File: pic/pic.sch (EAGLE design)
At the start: 33 parts, among them IC1 PIC16F877P, IC2 7805T, IC3 MAX233, Q1 16MHz, Q2 200MHz

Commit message: Schematic format update
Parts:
- added C7: 47μF, rcl:CPOL-EUE2.5-5
- added C8, C9: 15pF, rcl:CPOL-EUE2.5-5
- added F2: (no value), fuse:F457
- added IC4: 7805T, adafruit:7805T
- added IC5: MAX233, maxim:MAX233
- added J1: (no value), con-jack:JACK-PLUG1
- added J4: (no value), con-amp:520243-3
- added JP2: (no value), jumper:JP4Q
- added LED10: GREEN, adafruit:LED5MM
- added LED11: YELLOW, adafruit:LED5MM
- added LED12: RED, adafruit:LED5MM
- added LED7, LED8, LED9: (no value), adafruit:LED5MM
- added Q3: 16MHz, adafruit:CRYSTALHC49U-H
- added R11: 470, rcl:R-EU_0207/10
- added R12, R13: (no value), eagle-ltspice:R0207/10
- added R14: (no value), rcl:R-TRIMM3296X
- added R15, R16, R17, R18, R19: 470, eagle-ltspice:R0207/10
- added SW3, SW4: (no value), adafruit:SWITCH_PUSHBUTTONEVQ-PE
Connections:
- new net N$10: C7.+, IC4.VI, J1.3
- new net N$19: IC4.GND, J1.2
- new net N$20: F2.1, IC4.VO
- new net N$21: LED7.C, R11.2
- new net N$22: IC5G$1.R1IN, JP2.1, JP2.7
- new net N$23: IC5G$1.T1OUT, JP2.3, JP2.5
- new net N$24: J4.2, JP2.2, JP2.4
- new net N$25: J4.3, JP2.6, JP2.8
- new net N$26: IC5G$1.V-@1, IC5G$1.V-@2
- new net N$27: IC5G$1.C2-@1, IC5G$1.C2-@2
- new net N$28: IC5G$1.C2+@1, IC5G$1.C2+@2
- new net N$29: LED8.C, R15.1
- new net N$30: LED9.C, R16.1
- new net N$31: LED10.C, R17.1
- new net N$32: LED11.C, R18.1
- new net N$33: LED12.C, R19.1
- new net OSC3: C9.+, Q3.2
- new net OSC4: C8.+, Q3.1
- net A0: now also R14.S
- net A4: now also R13.1, SW4.P$2
- net A5: now also R17.2
- net B4: now also R18.2
- net B5: now also R19.2
- net C6: now also IC5G$1.T1IN
- net C7: now also IC5G$1.R1OUT
- net GND: now also C7.-, C8.-, C9.-, J4.5, R11.1, R14.E, SW3.P$1, SW4.P$1
- net LRX0: now also R16.2
- net LTX0: now also R15.2
- net RESET: now also R12.1, SW3.P$2
- net VCC: now also F2.2, LED10.A, LED11.A, LED12.A, LED7.A, LED8.A, LED9.A, R12.2, R13.2, R14.A

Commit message: 26/9/17 - LCD + PIC HEADER - EDITS TO RS232
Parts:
- removed J4: (no value), con-amp:520243-3
- removed SW3, SW4: (no value), adafruit:SWITCH_PUSHBUTTONEVQ-PE
- added C10: (no value), capacitor-wima:C5/5.5
- added C11, C12: 15pF, capacitor-wima:C5/5.5
- added C13: 1μF, rcl:CPOL-EUE2.5-5
- added IC6: PIC16F877P, microchip:PIC16F877P
- added J5: (no value), con-amp:520243-3
- added JP3: (no value), pinhead:PINHD-1X16
- added JP4: (no value), adafruit:PINHD-2X20
- added LED13: GREEN, adafruit:LED5MM
- added LED14: RED, adafruit:LED5MM
- added Q4: 200MHz, adafruit:CRYSTALHC49U-H
- added R20: 330, resistor:R-EU_0207/10
- added R21, R22: 470, resistor:R-EU_0207/10
- added R23: 10K, rcl:R-TRIMM3296X
- added R24: 100, eagle-ltspice:R0207/10
- added S1, S2: (no value), switch-omron:10-XX
- added X1: (no value), con-subd:F09HP
- R12, R13: value (none) -> 47K
- R14: value (none) -> 10K
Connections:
- removed net OSC3: C9.+, Q3.2
- removed net OSC4: C8.+, Q3.1
- new net 0SC1: JP4.14
- new net N$34: C12.2, Q4.1, R20.1
- new net N$35: LED13.A, R21.1
- new net N$36: LED14.A, R22.1
- new net N$38: JP3.3, R23.S
- new net N$45: JP3.15, R24.2
- new net N$46: C13.+, IC5P.VCC
- net A0: now also IC6.RA0/AN0, JP4.2
- net A1: now also IC6.RA1/AN1, JP4.3
- net A2: now also IC6.RA2/AN2, JP4.4
- net A3: now also IC6.RA3/AN3, JP4.5
- net A4: now also IC6.RA4/T0CKI, JP4.6, S2.S1; no longer SW4.P$2
- net A5: now also IC6.RA5/AN4, JP4.7
- net B0: now also IC6.INT/RB0, JP4.33
- net B1: now also IC6.RB1, JP4.34
- net B2: now also IC6.RB2, JP4.35
- net B3: now also IC6.PGM/RB3, JP4.36
- net B4: now also IC6.RB4, J5.4, JP4.37
- net B5: now also IC6.RB5, JP4.38
- net B6: now also IC6.PGC/RB6, J5.5, JP4.39
- net B7: now also IC6.PGD/RB7, J5.6, JP4.40
- net C0: now also IC6.RC0/T1OSO, JP4.15
- net C1: now also IC6.RC1/T1OSI, JP4.16
- net C2: now also IC6.RC2/CCP1, JP4.17
- net C3: now also IC6.RC3/SCK, JP4.18
- net C4: now also IC6.SDI/RC4, JP4.23
- net C5: now also IC6.SDO/RC5, JP4.24
- net C6: now also IC6.TX/RC6, JP4.25, LED13.C
- net C7: now also IC6.RX/RC7, JP4.26, LED14.C
- net D0: now also IC6.RD0/PSP0, JP3.6, JP4.19
- net D1: now also IC6.RD1/PSP1, JP3.4, JP4.20
- net D2: now also IC6.RD2/PSP2, JP3.5, JP4.21
- net D3: now also IC6.RD3/PSP3, JP4.22
- net D4: now also IC6.PSP4/RD4, JP3.11, JP4.27
- net D5: now also IC6.PSP5/RD5, JP3.12, JP4.28
- net D6: now also IC6.PSP6/RD6, JP3.13, JP4.29
- net D7: now also IC6.PSP7/RD7, JP3.14, JP4.30
- net E0: now also IC6.RE0/!RD/AN5, JP4.8
- net E1: now also IC6.RE1/!WR/AN6, JP4.9
- net E2: now also IC6.RE2/!CS/AN7, JP4.10
- net GND: now also C10.2, C11.1, C12.1, IC4.GND, IC6.VSS, IC6.VSS@1, J1.1, J1.2, J5.3, JP3.1, JP3.10, JP3.16, JP3.7, JP3.8, JP3.9, JP4.12, JP4.31, R21.2, R22.2, R23.A, S1.P1, S2.P1, X1.5; no longer J4.5, SW3.P$1, SW4.P$1
- net N$19: now also IC5P.GND@1, IC5P.GND@2; no longer IC4.GND, J1.2
- net N$24: now also X1.2; no longer J4.2
- net N$25: now also X1.3; no longer J4.3
- net OSC1: now also C11.2, C9.+, IC6.OSC1/CLKIN, Q3.2, Q4.2
- net OSC2: now also C8.+, IC6.OSC2/CLKOUT, JP4.13, Q3.1, R20.2
- net RESET: now also IC6.!MCLR/THV, J5.1, JP4.1, S1.S1; no longer SW3.P$2
- net VCC: now also C10.1, C13.-, IC6.VDD, IC6.VDD@1, J5.2, JP3.2, JP4.11, JP4.32, R23.E, R24.1

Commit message: Finished Schematic
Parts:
- removed C10: (no value), capacitor-wima:C5/5.5
- removed C11, C12: 15pF, capacitor-wima:C5/5.5
- removed C6: 15pF, rcl:CPOL-EUE2.5-5
- removed F1: (no value), fuse:F457
- removed IC2: 7805T, adafruit:7805T
- removed IC3: MAX233, maxim:MAX233
- removed IC6: PIC16F877P, microchip:PIC16F877P
- removed J2: (no value), con-amp:520243-3
- removed J3: (no value), con-jack:JACK-PLUG1
- removed LED1, LED2, LED3: (no value), adafruit:LED5MM
- removed LED4: GREEN, adafruit:LED5MM
- removed LED5: YELLOW, adafruit:LED5MM
- removed LED6: RED, adafruit:LED5MM
- removed Q1: 16MHz, adafruit:CRYSTALHC49U-H
- removed Q4: 200MHz, adafruit:CRYSTALHC49U-H
- removed R10, R6, R7, R8, R9: 470, eagle-ltspice:R0207/10
- removed R20: 330, resistor:R-EU_0207/10
- removed R3, R4: (no value), eagle-ltspice:R0207/10
- removed R5: (no value), rcl:R-TRIMM3296X
- removed SW1, SW2: (no value), adafruit:SWITCH_PUSHBUTTONEVQ-PE
- added IC7: PCA82C250, micro-philips:PCA82C250
- added U1: MCP2510P, microchip_can:MCP2510P
- added X2, X3: (no value), con-subd:F09HP
- C4: value 47μF -> 15μF
- C5: value 15pF -> 15μF
- JP1: device jumper:JP4Q -> jumper:JP1Q
- R2: device rcl:R-EU_0207/10 -> eagle-ltspice:R0207/10
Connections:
- removed net N$11: LED2.C, R6.1
- removed net N$12: IC3G$1.V-@1, IC3G$1.V-@2
- removed net N$13: IC3G$1.C2-@1, IC3G$1.C2-@2
- removed net N$14: IC3G$1.C2+@1, IC3G$1.C2+@2
- removed net N$15: LED3.C, R7.1
- removed net N$16: LED4.C, R8.1
- removed net N$17: LED5.C, R9.1
- removed net N$18: LED6.C, R10.1
- removed net N$34: C12.2, Q4.1, R20.1
- removed net N$5: IC3G$1.R1IN, JP1.1, JP1.7
- removed net N$6: LED1.C, R2.2
- removed net N$7: IC3G$1.T1OUT, JP1.3, JP1.5
- removed net N$8: J2.2, JP1.2, JP1.4
- removed net N$9: J2.3, JP1.6, JP1.8
- new net 0SC2: U1>NAME.OSC2
- net A0: no longer IC6.RA0/AN0, R5.S
- net A1: no longer IC6.RA1/AN1
- net A2: no longer IC6.RA2/AN2
- net A3: no longer IC6.RA3/AN3
- net A4: no longer IC6.RA4/T0CKI, R4.1, SW2.P$2
- net A5: no longer IC6.RA5/AN4, R8.2
- net B0: now also U1>NAME.INT; no longer IC6.INT/RB0
- net B1: no longer IC6.RB1
- net B2: no longer IC6.RB2
- net B3: no longer IC6.PGM/RB3
- net B4: no longer IC6.RB4, R9.2
- net B5: no longer IC6.RB5, R10.2
- net B6: no longer IC6.PGC/RB6
- net B7: no longer IC6.PGD/RB7
- net C0: no longer IC6.RC0/T1OSO
- net C1: no longer IC6.RC1/T1OSI
- net C2: now also U1>NAME.CS; no longer IC6.RC2/CCP1
- net C3: now also U1>NAME.SCK; no longer IC6.RC3/SCK
- net C4: now also U1>NAME.SO; no longer IC6.SDI/RC4
- net C5: now also U1>NAME.SI; no longer IC6.SDO/RC5
- net C6: no longer IC3G$1.T1IN, IC6.TX/RC6
- net C7: no longer IC3G$1.R1OUT, IC6.RX/RC7
- net D0: no longer IC6.RD0/PSP0
- net D1: no longer IC6.RD1/PSP1
- net D2: no longer IC6.RD2/PSP2
- net D3: no longer IC6.RD3/PSP3
- net D4: no longer IC6.PSP4/RD4
- net D5: no longer IC6.PSP5/RD5
- net D6: no longer IC6.PSP6/RD6
- net D7: no longer IC6.PSP7/RD7
- net E0: no longer IC6.RE0/!RD/AN5
- net E1: no longer IC6.RE1/!WR/AN6
- net E2: no longer IC6.RE2/!CS/AN7
- net GND: now also IC7.GND, IC7.RS, S1.P, S2.P, U1P.VSS, X2.6, X3.6; no longer C10.2, C11.1, C12.1, C6.-, IC6.VSS, IC6.VSS@1, J2.5, R2.1, R5.E, SW1.P$1, SW2.P$1
- net LRX0: now also IC7.TXD, U1>NAME.TXCAN; no longer R7.2
- net LTX0: now also IC7.RXD, U1>NAME.RXCAN; no longer R6.2
- net N$1: now also JP1.2, R2.2; no longer C4.+, IC2.VI, J3.3
- net N$3: now also IC7.CANL, R2.1, X2.2, X3.2; no longer IC2.GND, J3.2
- net N$4: now also IC7.CANH, JP1.1, X2.7, X3.7; no longer F1.1, IC2.VO
- net OSC1: now also U1>NAME.OSC1; no longer C11.2, C6.+, IC6.OSC1/CLKIN, Q1.2, Q4.2
- net OSC2: no longer C5.+, IC6.OSC2/CLKOUT, Q1.1, R20.2
- net RESET: now also S1.S, U1>NAME.RESET; no longer IC6.!MCLR/THV, R3.1, SW1.P$2
- net VCC: now also C4.+, C5.+, IC7.VCC, U1P.VDD, X2.9, X3.9; no longer C10.1, F1.2, IC6.VDD, IC6.VDD@1, LED1.A, LED2.A, LED3.A, LED4.A, LED5.A, LED6.A, R3.2, R4.2, R5.A

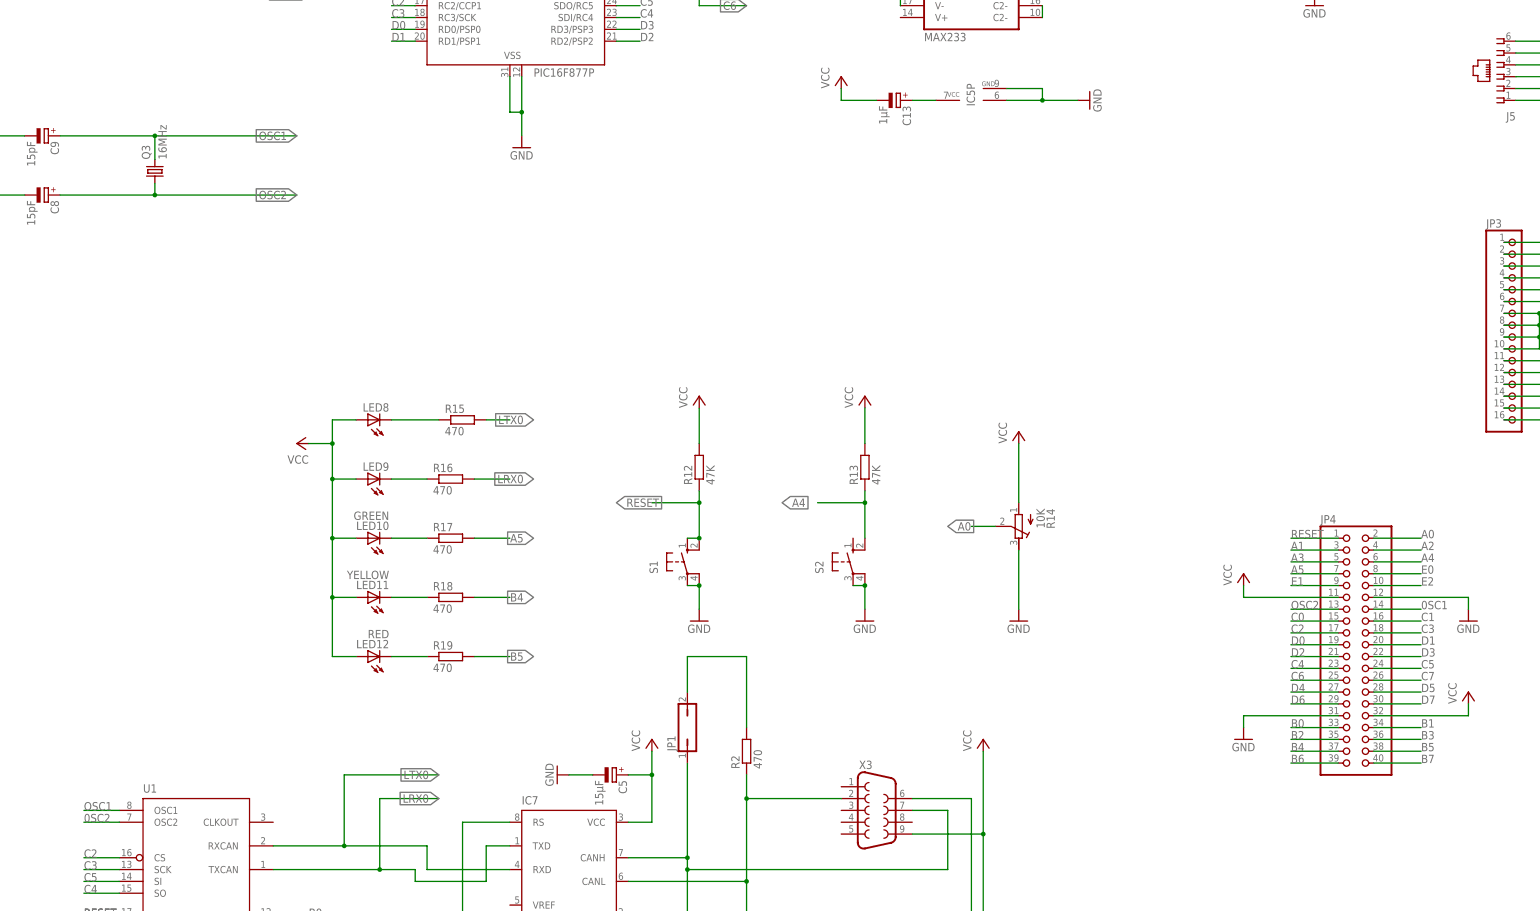
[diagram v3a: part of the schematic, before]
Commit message: Signed off netlist waiting check
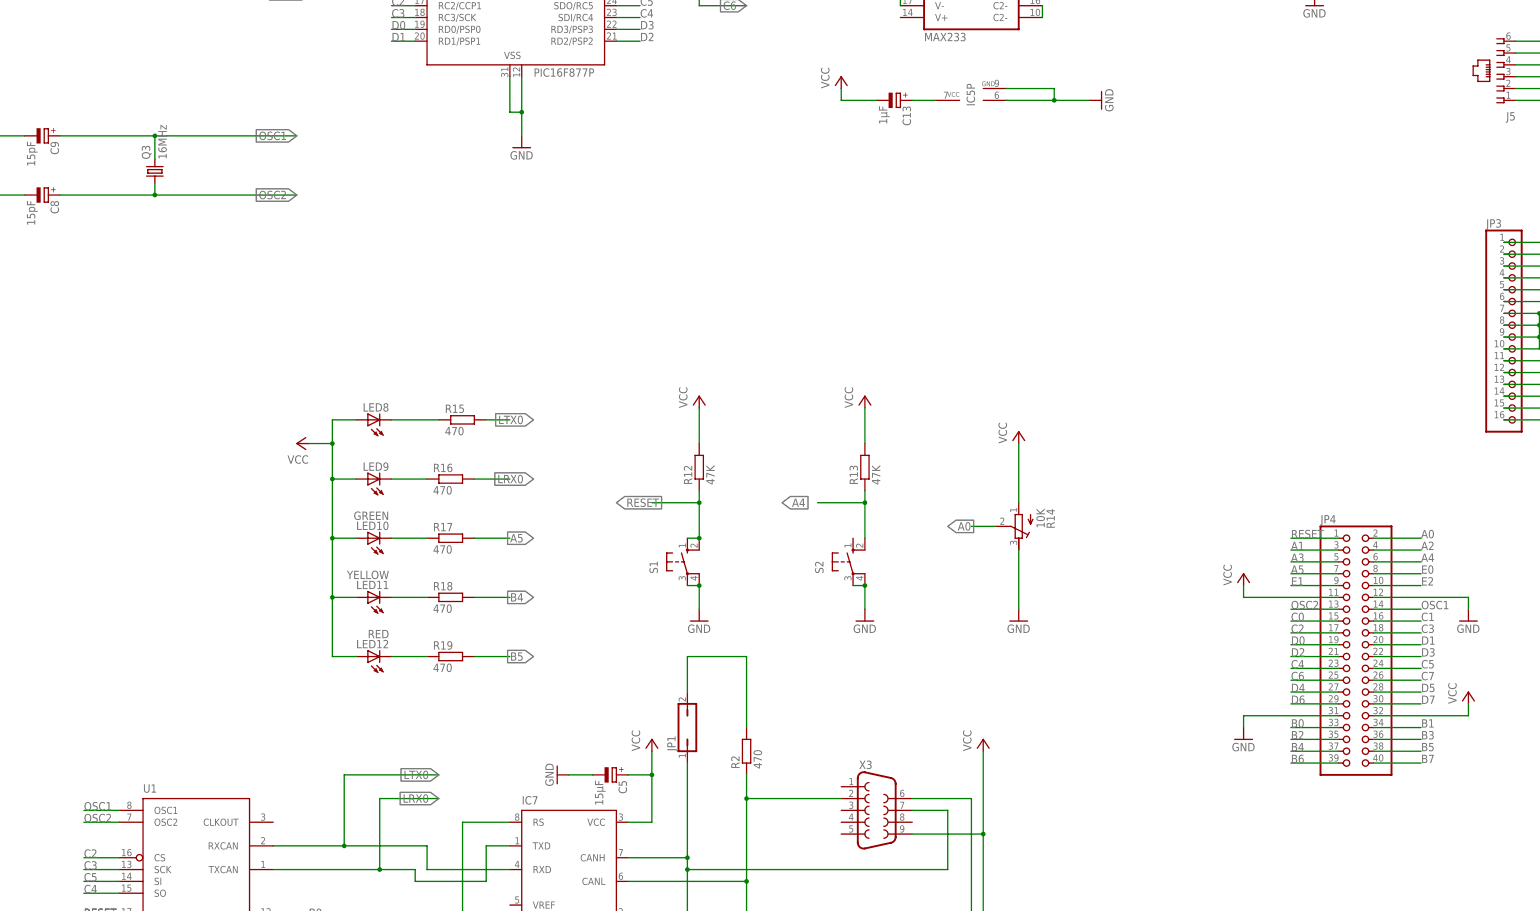
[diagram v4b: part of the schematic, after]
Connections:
- removed net 0SC1: JP4.14
- removed net 0SC2: U1>NAME.OSC2
- removed net N$19: IC5P.GND@1, IC5P.GND@2
- net GND: now also IC5P.GND@1, IC5P.GND@2
- net OSC1: now also JP4.14
- net OSC2: now also U1>NAME.OSC2
